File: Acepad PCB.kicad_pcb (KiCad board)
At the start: 2 copper layers, 139 x 76.2 mm, 65 parts, among them SW1 SW_Push, U1 ATmega32U4-AU, Y1 16MHz

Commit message: worked on pcb
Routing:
- net COL6: track 185.7 -> 238.9 mm
- net COL4: track 57.2 -> 107.7 mm, vias 0 -> 3
- net Net-(D2-Pad2): track 0.00 -> 10.2 mm
- net ROW0: track 137.7 -> 128.7 mm
- net Net-(D4-Pad2): track 0.00 -> 6.84 mm
- net Net-(D5-Pad2): track 0.00 -> 6.79 mm
- net Net-(D32-Pad2): track 0.00 -> 6.77 mm
- net Net-(D31-Pad2): track 0.00 -> 6.75 mm
- net Net-(D3-Pad2): track 0.00 -> 6.62 mm
- net Net-(R2-Pad1): track 27.2 -> 21.9 mm
- net Net-(R1-Pad1): track 23.4 -> 21.0 mm
- net COL0: track 109.9 -> 108.5 mm
- net ROW3: track 172.0 -> 173.5 mm
- net COL3: track 94.2 -> 94.9 mm
- net Net-(D25-Pad2): track 7.51 -> 6.82 mm
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
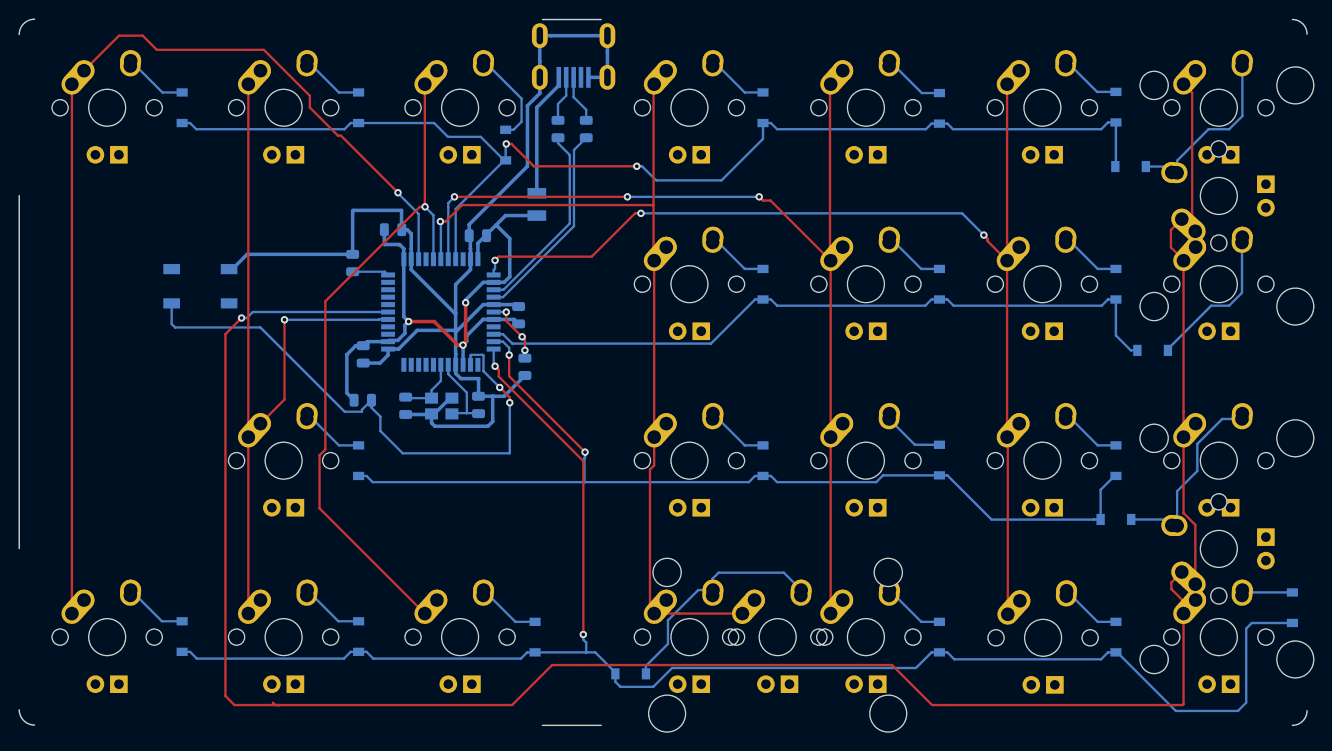
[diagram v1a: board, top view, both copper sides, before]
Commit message: continued work on pcb (flipped stabs, worked on wiring)
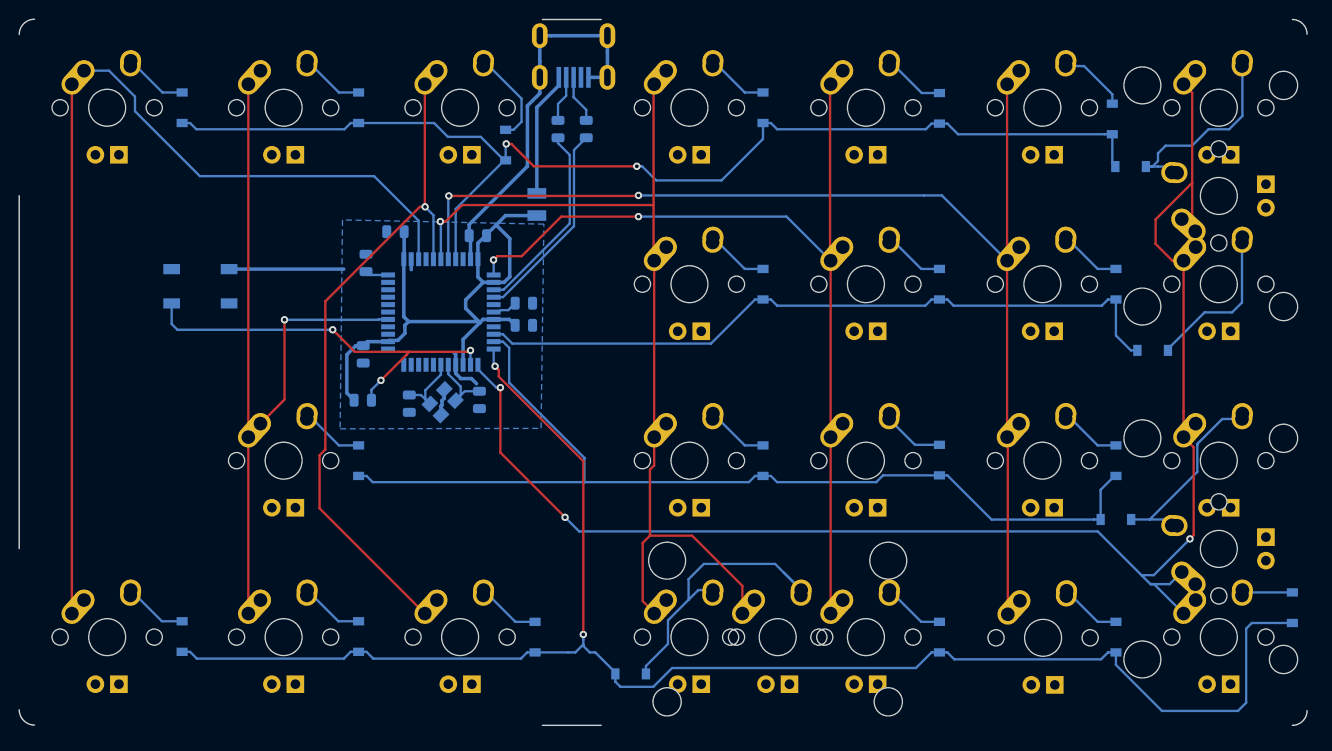
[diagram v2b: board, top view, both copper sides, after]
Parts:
- MX262, MX332, MX62: footprint MX_Alps_Hybrid:MX-2U -> MX_Alps_Hybrid:MX-2U-ReversedStabilizers
- moved C6 6.87 mm to (108.3, 110.8), turned to 0 degrees
- moved R4 1.44 mm to (91.3, 106.4)
- moved D5 1.33 mm to (171.9, 90.9)
- moved C5 1.23 mm to (108.3, 113.2), turned to 0 degrees
- moved C4 0.55 mm to (103.5, 121.2), turned to 270 degrees
- moved C3 0.46 mm to (96.0, 121.6)
- moved Y1 0.42 mm to (99.6, 121.5), turned to 45 degrees
- moved C1 0.34 mm to (94.5, 103.1), turned to 180 degrees
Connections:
- U1 pad 1: COL5 -> COL4
- U1 pad 12: Net-(U1-Pad12) -> COL6
- U1 pad 28: COL6 -> Net-(U1-Pad28)
- U1 pad 40: COL4 -> COL5
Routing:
- net GND: track 139.5 -> 62.6 mm
- net COL6: track 238.9 -> 163.3 mm, vias 1 -> 3
- net Net-(R3-Pad2): track 61.2 -> 44.3 mm, vias 2 -> 3
- net COL5: track 118.8 -> 127.6 mm, vias 3 -> 2
- net COL4: track 107.7 -> 99.1 mm, vias 3 -> 2
- net Net-(D33-Pad2): track 25.4 -> 32.4 mm
- net COL3: track 94.9 -> 101.3 mm
- net Net-(C6-Pad1): track 7.18 -> 2.72 mm, vias 3 -> 0
- net COL0: track 108.5 -> 105.1 mm, vias 1 -> 0
- net Net-(D6-Pad2): track 20.0 -> 22.8 mm
- net ROW0: track 128.7 -> 127.1 mm
- net Net-(R4-Pad2): track 3.97 -> 2.53 mm
- net Net-(C4-Pad1): track 8.61 -> 7.66 mm
- net Net-(C3-Pad1): track 6.86 -> 7.74 mm
- net +5V: track 69.4 -> 68.7 mm, vias 3 -> 0
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- added copper zone on B.Cu, net GND

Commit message: continued working on pcb
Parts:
- moved SW1 36.1 mm to (102.7, 130.1), turned to 180 degrees
- moved R3 17.9 mm to (108.5, 124.6)
- moved C5 2.48 mm to (109.2, 115.5), turned to 90 degrees
- moved D21 2.28 mm to (90.4, 130.1)
- moved C6 1.98 mm to (109.0, 112.7)
- moved C4 1.33 mm to (103.7, 122.6)
- moved C3 1.13 mm to (95.8, 122.8)
- moved Y1 0.99 mm to (99.6, 122.5)
- moved C1 0.36 mm to (94.2, 103.3), turned to 90 degrees
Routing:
- net GND: track 62.6 -> 111.1 mm
- net Net-(R3-Pad2): track 44.3 -> 17.6 mm, vias 3 -> 0
- net +5V: track 68.7 -> 87.1 mm, vias 0 -> 5
- net ROW1: track 77.5 -> 81.0 mm
- net ROW2: track 108.5 -> 111.2 mm
- net Net-(C6-Pad1): track 2.72 -> 3.90 mm
- net Net-(C4-Pad1): track 7.66 -> 8.67 mm
- net COL4: track 99.1 -> 98.2 mm
- net Net-(D21-Pad2): track 6.77 -> 7.60 mm
- net Net-(C3-Pad1): track 7.74 -> 8.42 mm
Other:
- outline, holes or cut-outs redrawn
- board text added: "Acepad V1.0"
